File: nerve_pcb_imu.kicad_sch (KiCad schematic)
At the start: 16 parts, among them U3 BNO085, Y3 32k768

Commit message: Simplify clock circuits
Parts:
- renumbered R14 to R11, R15 to R12, R16 to R13, R17 to R14, R18 to R15, R19 to R16, R20 to R17, R21 to R18
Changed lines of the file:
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@@
 		(on_board yes)
 		(dnp no)
-		(property "Reference" "R20"
+		(property "Reference" "R17"
 			(at 230.124 106.68 0)
 			(effects
@@
 			(project "nerve_pcb"
 				(path "/c0277862-b3f2-4e0e-986f-34702f0543f0/1178a2c5-f6af-4893-bc81-c8b9cb81f032"
-					(reference "R20")
+					(reference "R17")
 					(unit 1)
 				)
@@
 		(on_board yes)
 		(dnp no)
-		(property "Reference" "R18"
+		(property "Reference" "R15"
 			(at 93.726 106.68 0)
 			(effects
@@
 			(project "nerve_pcb"
 				(path "/c0277862-b3f2-4e0e-986f-34702f0543f0/1178a2c5-f6af-4893-bc81-c8b9cb81f032"
-					(reference "R18")
+					(reference "R15")
 					(unit 1)
 				)
@@
 		(on_board yes)
 		(dnp no)
-		(property "Reference" "R21"
+		(property "Reference" "R18"
 			(at 122.936 113.03 0)
 			(effects
@@
 			(project "nerve_pcb"
 				(path "/c0277862-b3f2-4e0e-986f-34702f0543f0/1178a2c5-f6af-4893-bc81-c8b9cb81f032"
-					(reference "R21")
+					(reference "R18")
 					(unit 1)
 				)
@@
 		(on_board yes)
 		(dnp no)
-		(property "Reference" "R15"
+		(property "Reference" "R12"
 			(at 122.174 86.36 0)
 			(effects
@@
 			(project "nerve_pcb"
 				(path "/c0277862-b3f2-4e0e-986f-34702f0543f0/1178a2c5-f6af-4893-bc81-c8b9cb81f032"
-					(reference "R15")
+					(reference "R12")
 					(unit 1)
 				)
@@
 		(on_board yes)
 		(dnp no)
-		(property "Reference" "R17"
+		(property "Reference" "R14"
 			(at 188.976 104.14 0)
 			(effects
@@
 			(project "nerve_pcb"
 				(path "/c0277862-b3f2-4e0e-986f-34702f0543f0/1178a2c5-f6af-4893-bc81-c8b9cb81f032"
-					(reference "R17")
+					(reference "R14")
 					(unit 1)
 				)
@@
 		(on_board yes)
 		(dnp no)
-		(property "Reference" "R14"
+		(property "Reference" "R11"
 			(at 109.474 86.36 0)
 			(effects
@@
 			(project "nerve_pcb"
 				(path "/c0277862-b3f2-4e0e-986f-34702f0543f0/1178a2c5-f6af-4893-bc81-c8b9cb81f032"
-					(reference "R14")
+					(reference "R11")
 					(unit 1)
 				)
@@
 		(on_board yes)
 		(dnp no)
-		(property "Reference" "R16"
+		(property "Reference" "R13"
 			(at 134.874 86.36 0)
 			(effects
@@
 			(project "nerve_pcb"
 				(path "/c0277862-b3f2-4e0e-986f-34702f0543f0/1178a2c5-f6af-4893-bc81-c8b9cb81f032"
-					(reference "R16")
+					(reference "R13")
 					(unit 1)
 				)
@@
 		(on_board yes)
 		(dnp no)
-		(property "Reference" "R19"
+		(property "Reference" "R16"
 			(at 214.122 106.68 0)
 			(effects
@@
 			(project "nerve_pcb"
 				(path "/c0277862-b3f2-4e0e-986f-34702f0543f0/1178a2c5-f6af-4893-bc81-c8b9cb81f032"
-					(reference "R19")
-					(unit 1)
-				)
+					(reference "R16")
+					(unit 1)
+				)

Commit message: Update IMU clock circuit and cleanup
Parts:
- removed R16, R17: 0R, Resistor_SMD:R_0603_1608Metric, symbol Device:R
- renumbered R18 to R16
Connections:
- net at C20.1, Y3.2: now also U3.26 (XOUT32/CLKSEL1)
- net at U3.27 (XIN32): now also C19.1, Y3.1
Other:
- moved on the sheet: C19, C20, Y3

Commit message: Swap 32k768 crystal caps to 18pF
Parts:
- C19, C20: value 15p -> 18p
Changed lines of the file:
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@@
 			)
 		)
-		(property "Value" "15p"
+		(property "Value" "18p"
 			(at 231.14 115.57 0)
 			(effects
@@
 			)
 		)
-		(property "Value" "15p"
+		(property "Value" "18p"
 			(at 213.36 115.57 0)
 			(effects

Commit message: Add WS2812Bs
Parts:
- renumbered U3 to U4
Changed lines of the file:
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@@
 		(dnp no)
 		(fields_autoplaced yes)
-		(property "Reference" "#PWR062"
+		(property "Reference" "#PWR069"
 			(at 153.67 142.24 0)
 			(effects
@@
 			(project "nerve_pcb"
 				(path "/c0277862-b3f2-4e0e-986f-34702f0543f0/1178a2c5-f6af-4893-bc81-c8b9cb81f032"
-					(reference "#PWR062")
+					(reference "#PWR069")
 					(unit 1)
 				)
@@
 		(dnp no)
 		(fields_autoplaced yes)
-		(property "Reference" "#PWR059"
+		(property "Reference" "#PWR066"
 			(at 124.46 125.73 0)
 			(effects
@@
 			(project "nerve_pcb"
 				(path "/c0277862-b3f2-4e0e-986f-34702f0543f0/1178a2c5-f6af-4893-bc81-c8b9cb81f032"
-					(reference "#PWR059")
+					(reference "#PWR066")
 					(unit 1)
 				)
@@
 		(dnp no)
 		(fields_autoplaced yes)
-		(property "Reference" "#PWR058"
+		(property "Reference" "#PWR065"
 			(at 95.25 119.38 0)
 			(effects
@@
 			(project "nerve_pcb"
 				(path "/c0277862-b3f2-4e0e-986f-34702f0543f0/1178a2c5-f6af-4893-bc81-c8b9cb81f032"
-					(reference "#PWR058")
+					(reference "#PWR065")
 					(unit 1)
 				)
@@
 		(on_board yes)
 		(dnp no)
-		(property "Reference" "U3"
+		(property "Reference" "U4"
 			(at 175.006 84.328 0)
 			(effects
@@
 			(project ""
 				(path "/c0277862-b3f2-4e0e-986f-34702f0543f0/1178a2c5-f6af-4893-bc81-c8b9cb81f032"
-					(reference "U3")
+					(reference "U4")
 					(unit 1)
 				)
@@
 		(on_board yes)
 		(dnp no)
-		(property "Reference" "#PWR054"
+		(property "Reference" "#PWR061"
 			(at 120.65 86.36 0)
 			(effects
@@
 			(project "nerve_pcb"
 				(path "/c0277862-b3f2-4e0e-986f-34702f0543f0/1178a2c5-f6af-4893-bc81-c8b9cb81f032"
-					(reference "#PWR054")
+					(reference "#PWR061")
 					(unit 1)
 				)
@@
 		(dnp no)
 		(fields_autoplaced yes)
-		(property "Reference" "#PWR061"
+		(property "Reference" "#PWR068"
 			(at 160.02 134.62 0)
 			(effects
@@
 			(project "nerve_pcb"
 				(path "/c0277862-b3f2-4e0e-986f-34702f0543f0/1178a2c5-f6af-4893-bc81-c8b9cb81f032"
-					(reference "#PWR061")
+					(reference "#PWR068")
 					(unit 1)
 				)
@@
 		(dnp no)
 		(fields_autoplaced yes)
-		(property "Reference" "#PWR057"
+		(property "Reference" "#PWR064"
 			(at 190.5 116.84 0)
 			(effects
@@
 			(project "nerve_pcb"
 				(path "/c0277862-b3f2-4e0e-986f-34702f0543f0/1178a2c5-f6af-4893-bc81-c8b9cb81f032"
-					(reference "#PWR057")
+					(reference "#PWR064")
 					(unit 1)
 				)
@@
 		(dnp no)
 		(fields_autoplaced yes)
-		(property "Reference" "#PWR052"
+		(property "Reference" "#PWR059"
 			(at 177.8 82.55 0)
 			(effects
@@
 			(project "nerve_pcb"
 				(path "/c0277862-b3f2-4e0e-986f-34702f0543f0/1178a2c5-f6af-4893-bc81-c8b9cb81f032"
-					(reference "#PWR052")
+					(reference "#PWR059")
 					(unit 1)
 				)
@@
 		(on_board yes)
 		(dnp no)
-		(property "Reference" "#PWR055"
+		(property "Reference" "#PWR062"
 			(at 133.35 86.36 0)
 			(effects
@@
 			(project "nerve_pcb"
 				(path "/c0277862-b3f2-4e0e-986f-34702f0543f0/1178a2c5-f6af-4893-bc81-c8b9cb81f032"
-					(reference "#PWR055")
+					(reference "#PWR062")
 					(unit 1)
 				)
@@
 		(dnp no)
 		(fields_autoplaced yes)
-		(property "Reference" "#PWR060"
+		(property "Reference" "#PWR067"
 			(at 222.25 128.27 0)
 			(effects
@@
 			(project "nerve_pcb"
 				(path "/c0277862-b3f2-4e0e-986f-34702f0543f0/1178a2c5-f6af-4893-bc81-c8b9cb81f032"
-					(reference "#PWR060")
+					(reference "#PWR067")
 					(unit 1)
 				)
@@
 		(on_board yes)
 		(dnp no)
-		(property "Reference" "#PWR053"
+		(property "Reference" "#PWR060"
 			(at 107.95 86.36 0)
 			(effects
@@
 			(project "nerve_pcb"
 				(path "/c0277862-b3f2-4e0e-986f-34702f0543f0/1178a2c5-f6af-4893-bc81-c8b9cb81f032"
-					(reference "#PWR053")
+					(reference "#PWR060")
 					(unit 1)
 				)
@@
 		(on_board yes)
 		(dnp no)
-		(property "Reference" "#PWR051"
+		(property "Reference" "#PWR058"
 			(at 177.8 67.31 0)
 			(effects
@@
 			(project "nerve_pcb"
 				(path "/c0277862-b3f2-4e0e-986f-34702f0543f0/1178a2c5-f6af-4893-bc81-c8b9cb81f032"
-					(reference "#PWR051")
+					(reference "#PWR058")
 					(unit 1)
 				)
@@
 		(on_board yes)
 		(dnp no)
-		(property "Reference" "#PWR056"
+		(property "Reference" "#PWR063"
 			(at 198.12 100.33 0)
 			(effects
@@
 			(project "nerve_pcb"
 				(path "/c0277862-b3f2-4e0e-986f-34702f0543f0/1178a2c5-f6af-4893-bc81-c8b9cb81f032"
-					(reference "#PWR056")
-					(unit 1)
-				)
+					(reference "#PWR063")
+					(unit 1)
+				)

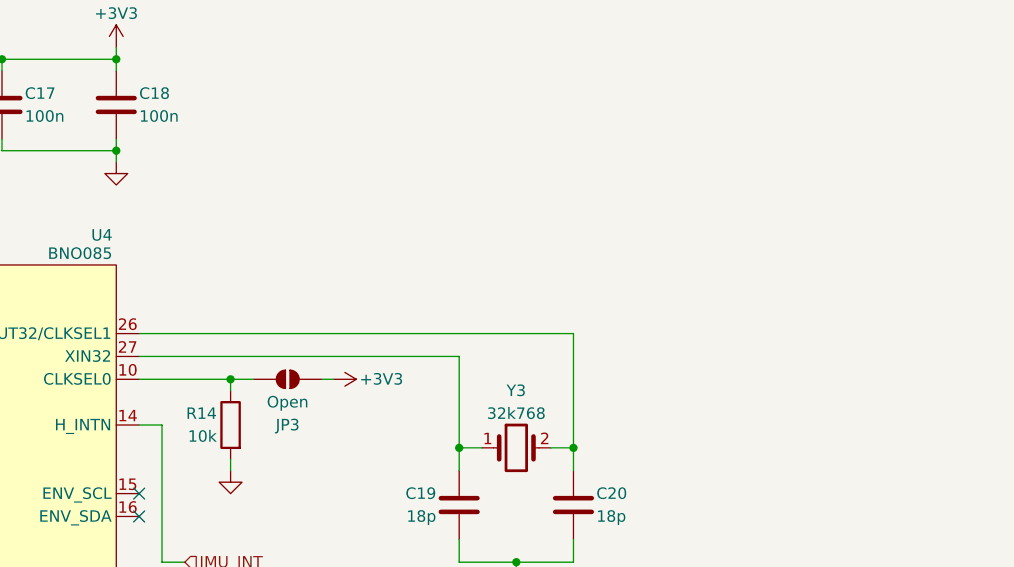
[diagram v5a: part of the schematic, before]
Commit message: Add design notes on schematic
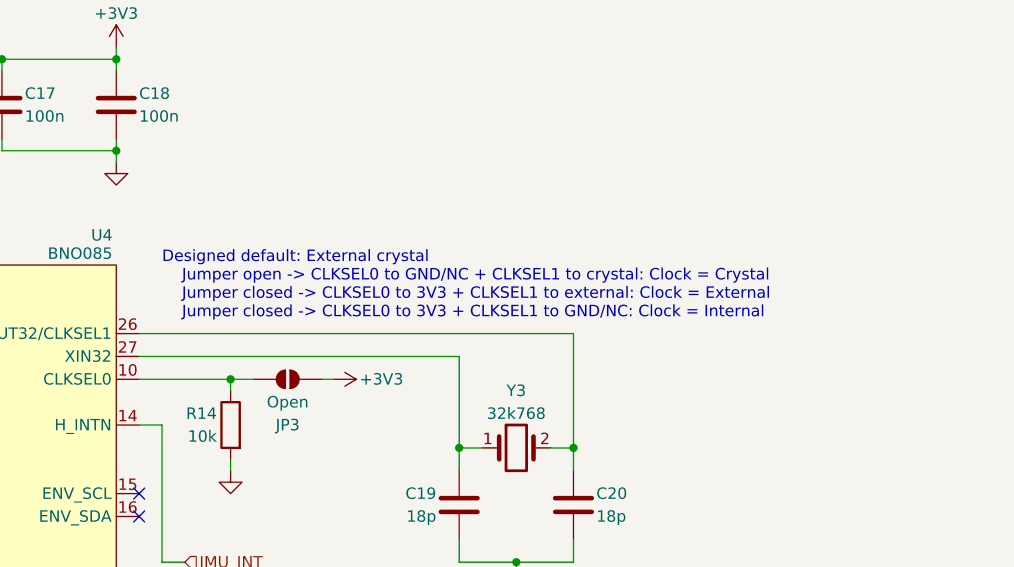
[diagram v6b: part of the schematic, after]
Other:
- note added: "Designed default: External crystal Jumper open -> CLKSEL0 to GND/NC + CLKSEL1 to crystal: Clock = Crystal Jumper closed -> CLKSEL0 to 3V3 + CLKSEL1 to external: Clock = External Jumper closed -> CLKSEL0 to 3V3 + CLKSEL1 to GND/NC: Clock = Internal"
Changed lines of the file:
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@@
+		)
+	)
+	(text "Designed default: External crystal\n    Jumper open -> CLKSEL0 to GND/NC + CLKSEL1 to crystal: Clock = Crystal\n    Jumper closed -> CLKSEL0 to 3V3 + CLKSEL1 to external: Clock = External\n    Jumper closed -> CLKSEL0 to 3V3 + CLKSEL1 to GND/NC: Clock = Internal"
+		(exclude_from_sim no)
+		(at 182.88 89.916 0)
+		(effects
+			(font
+				(size 1.27 1.27)
+				(thickness 0.1588)
+			)
+			(justify left)
 		)
 	)

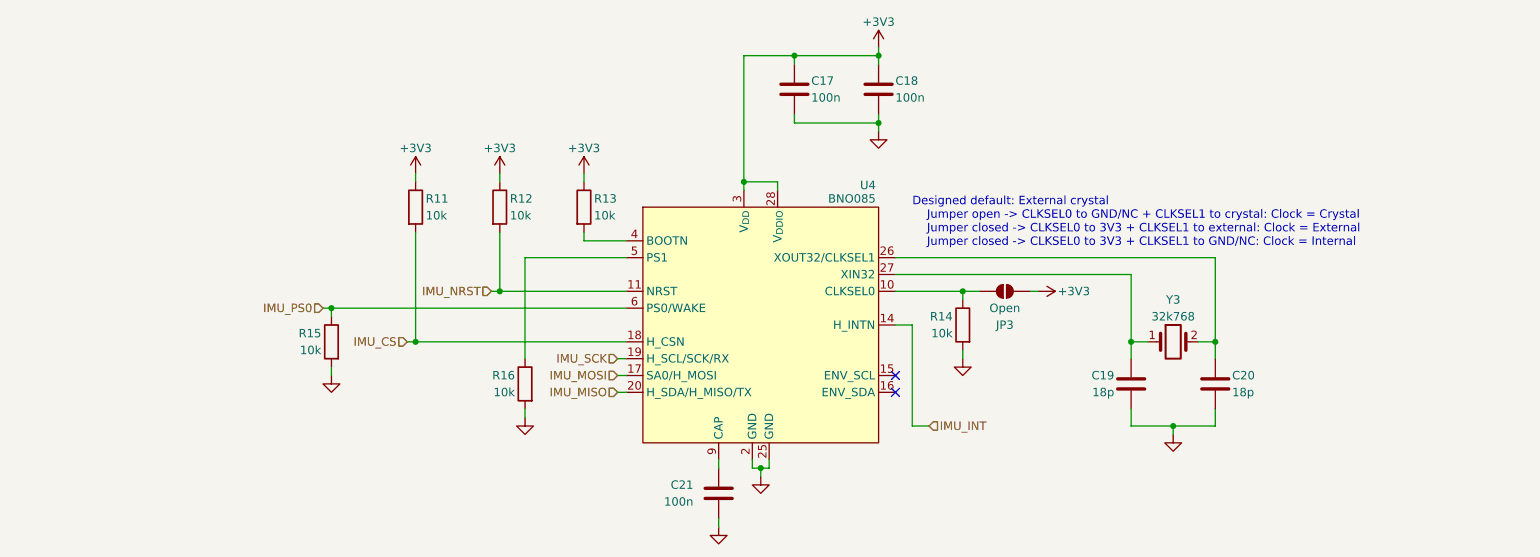
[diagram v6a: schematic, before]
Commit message: Fix BNO085 circuit for SPI
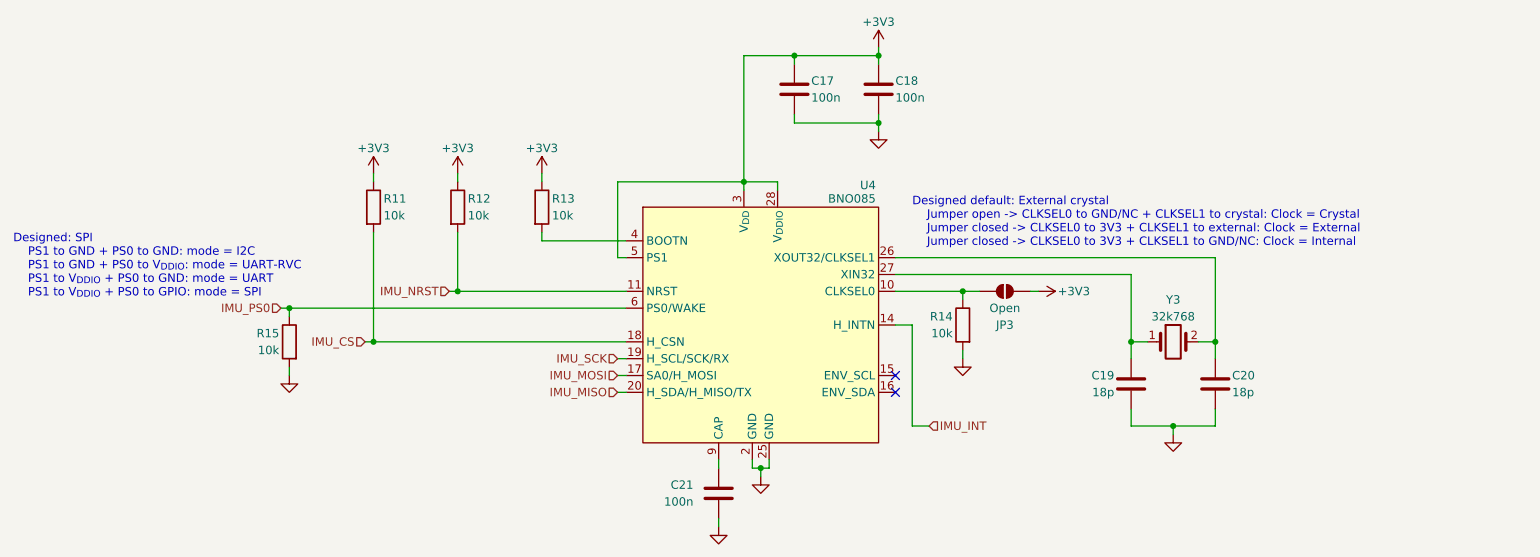
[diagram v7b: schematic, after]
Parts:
- removed R16: 10k, Resistor_SMD:R_0603_1608Metric, symbol Device:R
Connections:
- net +3V3: now also U4.5 (PS1)
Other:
- note added: "Designed: SPI PS1 to GND + PS0 to GND: mode = I2C PS1 to GND + PS0 to V_{DDIO}: mode = UART-RVC PS1 to V_{DDIO} + PS0 to GND: mode = UART PS1 to V_{DDIO} + PS0 to GPIO: mode = SPI"
- moved on the sheet: R11, R12, R13, R15
